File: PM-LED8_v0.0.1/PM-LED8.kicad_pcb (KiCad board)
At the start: 2 copper layers, 29.8 x 99.8 mm, 26 parts, among them J1 AFA07-S10FCC-00, J2 AFA07-S10FCC-00, J3 AFA07-S10FCC-00, J4 AFA07-S10FCC-00

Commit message: update
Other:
- outline, holes or cut-outs redrawn
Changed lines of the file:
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@@
 		(pad_to_mask_clearance 0)
 		(allow_soldermask_bridges_in_footprints no)
-		(grid_origin 60.72 80.48)
+		(aux_axis_origin 65.8 100.8)
+		(grid_origin 65.8 100.8)
 		(pcbplotparams
 			(layerselection 0x00010fc_ffffffff)
@@
 		(layer "Cmts.User")
 	)
+	(gr_arc
+		(start 50.9 54.8)
+		(mid 52.042284 52.042284)
+		(end 54.8 50.9)
+		(stroke
+			(width 0.2)
+			(type default)
+		)
+		(layer "Edge.Cuts")
+	)
 	(gr_line
 		(start 64.8 53.8)
@@
 	(gr_line
 		(start 61.9 150.7)
-		(end 53.8 150.7)
+		(end 54.8 150.7)
 		(stroke
 			(width 0.2)
@@
 	)
 	(gr_line
-		(start 50.9 147.8)
-		(end 50.9 53.8)
+		(start 50.9 146.8)
+		(end 50.9 54.8)
 		(stroke
 			(width 0.2)
@@
 		(layer "Edge.Cuts")
 	)
-	(gr_arc
-		(start 53.8 150.7)
-		(mid 51.74939 149.85061)
-		(end 50.9 147.8)
-		(stroke
-			(width 0.2)
-			(type default)
-		)
-		(layer "Edge.Cuts")
-	)
 	(gr_line
 		(start 80.7 53.8)
@@
 		(layer "Edge.Cuts")
 	)
-	(gr_arc
-		(start 50.9 53.8)
-		(mid 51.74939 51.74939)
-		(end 53.8 50.9)
-		(stroke
-			(width 0.2)
-			(type default)
-		)
-		(layer "Edge.Cuts")
-	)
 	(gr_line
 		(start 72.8 54.85)
@@
 	)
 	(gr_line
-		(start 53.8 50.9)
+		(start 54.8 50.9)
 		(end 61.9 50.9)
 		(stroke
@@
 		(stroke
 			(width 0.2)
+			(type default)
+		)
+		(layer "Edge.Cuts")
+	)
+	(gr_arc
+		(start 54.8 150.7)
+		(mid 52.042284 149.557716)
+		(end 50.9 146.8)
+		(stroke
+			(width 0.2)

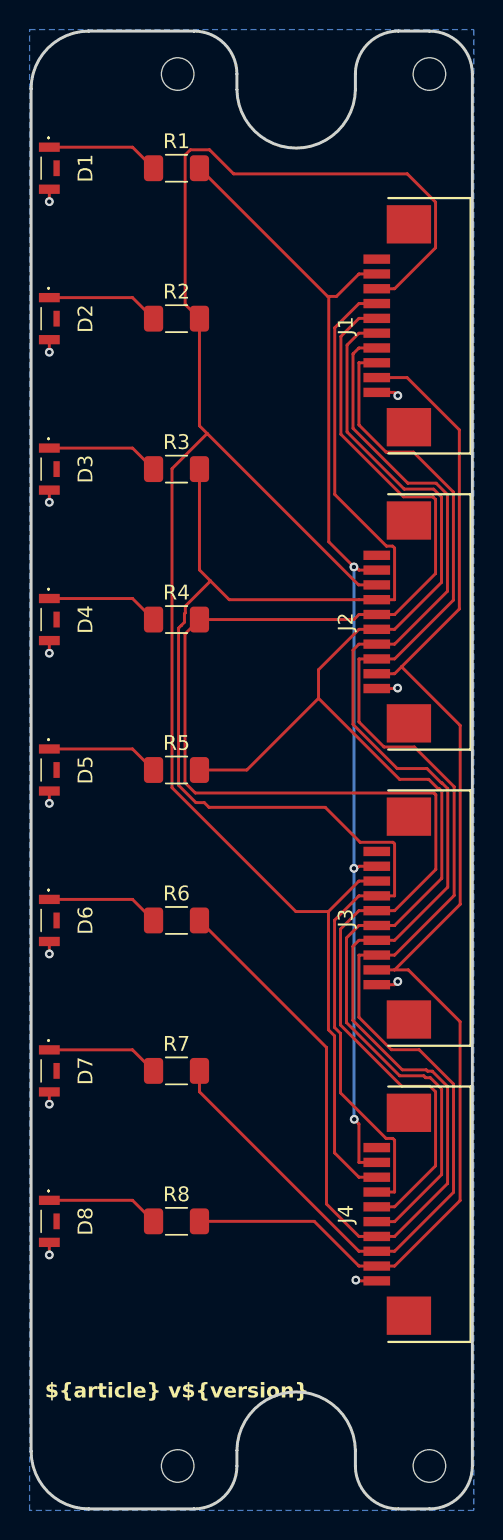
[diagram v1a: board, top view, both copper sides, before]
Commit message: update new size
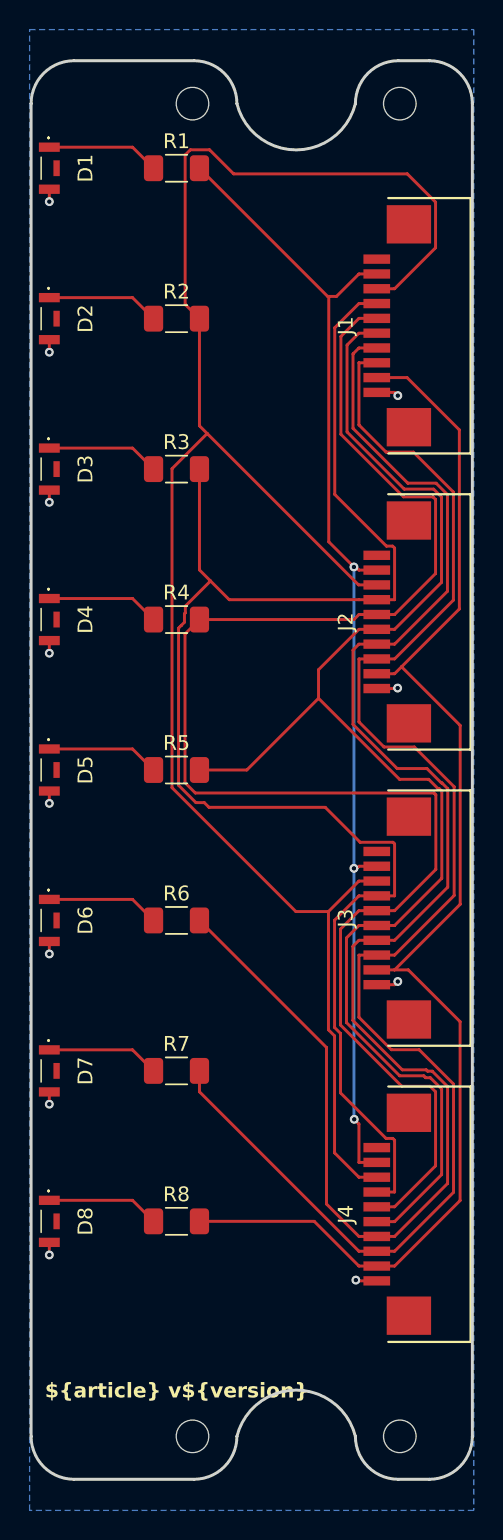
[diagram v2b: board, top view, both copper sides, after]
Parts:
- moved H1 2.83 mm to (75.8, 55.8)
- moved H2 2.83 mm to (75.8, 145.8)
- moved H3 2.24 mm to (61.8, 55.8)
- moved H4 2.24 mm to (61.8, 145.8)
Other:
- board size 29.8 x 99.8 mm -> 29.8 x 95.8 mm
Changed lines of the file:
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@@
 	(footprint "MountingHole:MountingHole_2.2mm_M2"
 		(layer "F.Cu")
-		(at 77.8 53.8)
+		(at 75.8 55.8)
 		(descr "Mounting Hole 2.2mm, no annular, M2")
 		(tags "mounting hole 2.2mm no annular m2")
@@
 	(footprint "MountingHole:MountingHole_2.2mm_M2"
 		(layer "F.Cu")
-		(at 60.8 147.8)
+		(at 61.8 145.8)
 		(descr "Mounting Hole 2.2mm, no annular, M2")
 		(tags "mounting hole 2.2mm no annular m2")
@@
 	(footprint "MountingHole:MountingHole_2.2mm_M2"
 		(layer "F.Cu")
-		(at 77.8 147.8)
+		(at 75.8 145.8)
 		(descr "Mounting Hole 2.2mm, no annular, M2")
 		(tags "mounting hole 2.2mm no annular m2")
@@
 	(footprint "MountingHole:MountingHole_2.2mm_M2"
 		(layer "F.Cu")
-		(at 60.8 53.8)
+		(at 61.8 55.8)
 		(descr "Mounting Hole 2.2mm, no annular, M2")
 		(tags "mounting hole 2.2mm no annular m2")
@@
 		(layer "Cmts.User")
 	)
-	(gr_arc
-		(start 50.9 54.8)
-		(mid 52.042284 52.042284)
-		(end 54.8 50.9)
-		(stroke
-			(width 0.2)
-			(type default)
-		)
-		(layer "Edge.Cuts")
-	)
 	(gr_line
-		(start 64.8 53.8)
-		(end 64.8 54.85)
+		(start 50.9 145.8)
+		(end 50.9 55.8)
 		(stroke
 			(width 0.2)
@@
 	)
 	(gr_arc
-		(start 77.8 50.9)
-		(mid 79.85061 51.74939)
-		(end 80.7 53.8)
-		(stroke
-			(width 0.2)
-			(type default)
-		)
-		(layer "Edge.Cuts")
-	)
-	(gr_line
-		(start 61.9 150.7)
-		(end 54.8 150.7)
+		(start 77.8 52.9)
+		(mid 79.85061 53.74939)
+		(end 80.7 55.8)
 		(stroke
 			(width 0.2)
@@
 	)
 	(gr_arc
-		(start 61.9 50.9)
-		(mid 63.95061 51.74939)
-		(end 64.8 53.8)
+		(start 64.800001 145.8)
+		(mid 68.8 142.676895)
+		(end 72.799999 145.8)
 		(stroke
 			(width 0.2)
@@
 		(layer "Edge.Cuts")
 	)
-	(gr_line
-		(start 64.8 146.75)
-		(end 64.8 147.8)
+	(gr_arc
+		(start 53.8 148.7)
+		(mid 51.74939 147.85061)
+		(end 50.9 145.8)
 		(stroke
 			(width 0.2)
@@
 	)
 	(gr_arc
-		(start 80.7 147.8)
-		(mid 79.85061 149.85061)
-		(end 77.8 150.7)
+		(start 72.8 55.8)
+		(mid 73.64939 53.74939)
+		(end 75.7 52.9)
 		(stroke
 			(width 0.2)
@@
 	)
 	(gr_line
-		(start 50.9 146.8)
-		(end 50.9 54.8)
+		(start 77.8 148.7)
+		(end 75.7 148.7)
 		(stroke
 			(width 0.2)
@@
 		(layer "Edge.Cuts")
 	)
-	(gr_line
-		(start 72.8 147.8)
-		(end 72.8 146.75)
+	(gr_arc
+		(start 75.7 148.7)
+		(mid 73.64939 147.85061)
+		(end 72.8 145.8)
 		(stroke
 			(width 0.2)
@@
 	)
 	(gr_arc
-		(start 72.8 54.85)
-		(mid 68.8 58.800312)
-		(end 64.8 54.85)
+		(start 72.799999 55.8)
+		(mid 68.8 58.923105)
+		(end 64.800001 55.8)
 		(stroke
 			(width 0.2)
@@
 	)
 	(gr_line
-		(start 77.8 150.7)
-		(end 75.7 150.7)
-		(stroke
-			(width 0.2)
-			(type default)
-		)
-		(layer "Edge.Cuts")
-	)
-	(gr_arc
-		(start 64.8 147.8)
-		(mid 63.95061 149.85061)
-		(end 61.9 150.7)
+		(start 80.7 55.8)
+		(end 80.7 145.8)
 		(stroke
 			(width 0.2)
@@
 	)
 	(gr_arc
-		(start 72.8 53.8)
-		(mid 73.64939 51.74939)
-		(end 75.7 50.9)
+		(start 80.7 145.8)
+		(mid 79.85061 147.85061)
+		(end 77.8 148.7)
 		(stroke
 			(width 0.2)
@@
 	)
 	(gr_line
-		(start 80.7 53.8)
-		(end 80.7 147.8)
+		(start 61.9 148.7)
+		(end 53.8 148.7)
 		(stroke
 			(width 0.2)
@@
 	)
 	(gr_line
-		(start 72.8 54.85)
-		(end 72.8 53.8)
+		(start 61.9 52.9)
+		(end 53.8 52.9)
 		(stroke
 			(width 0.2)
@@
 	)
 	(gr_arc
-		(start 75.7 150.7)
-		(mid 73.64939 149.85061)
-		(end 72.8 147.8)
-		(stroke
-			(width 0.2)
-			(type default)
-		)
-		(layer "Edge.Cuts")
-	)
-	(gr_line
-		(start 75.7 50.9)
-		(end 77.8 50.9)
+		(start 50.9 55.8)
+		(mid 51.74939 53.74939)
+		(end 53.8 52.9)
 		(stroke
 			(width 0.2)
@@
 	)
 	(gr_line
-		(start 54.8 50.9)
-		(end 61.9 50.9)
+		(start 77.8 52.9)
+		(end 75.7 52.9)
 		(stroke
 			(width 0.2)
@@
 	)
 	(gr_arc
-		(start 64.8 146.75)
-		(mid 68.8 142.799688)
-		(end 72.8 146.75)
+		(start 61.9 52.9)
+		(mid 63.95061 53.74939)
+		(end 64.8 55.8)
 		(stroke
 			(width 0.2)
@@
 	)
 	(gr_arc
-		(start 54.8 150.7)
-		(mid 52.042284 149.557716)
-		(end 50.9 146.8)
+		(start 64.8 145.8)
+		(mid 63.95061 147.85061)
+		(end 61.9 148.7)
 		(stroke
 			(width 0.2)
